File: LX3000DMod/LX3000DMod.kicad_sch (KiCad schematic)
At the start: 0 parts

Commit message: audio input terminado
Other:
- added sheet AudioSignals (AudioSignals.kicad_sch)

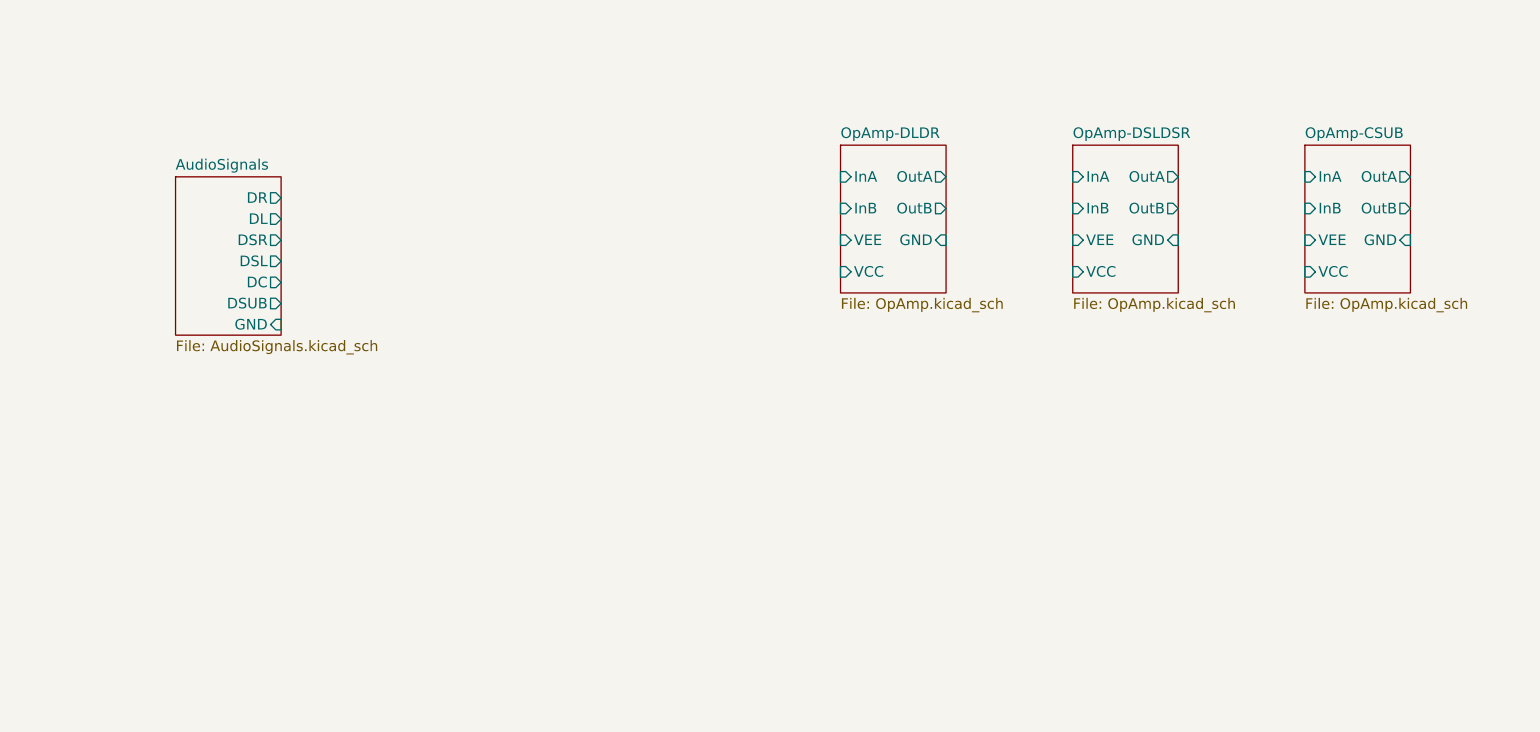
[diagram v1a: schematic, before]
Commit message: 10.8 PSU done
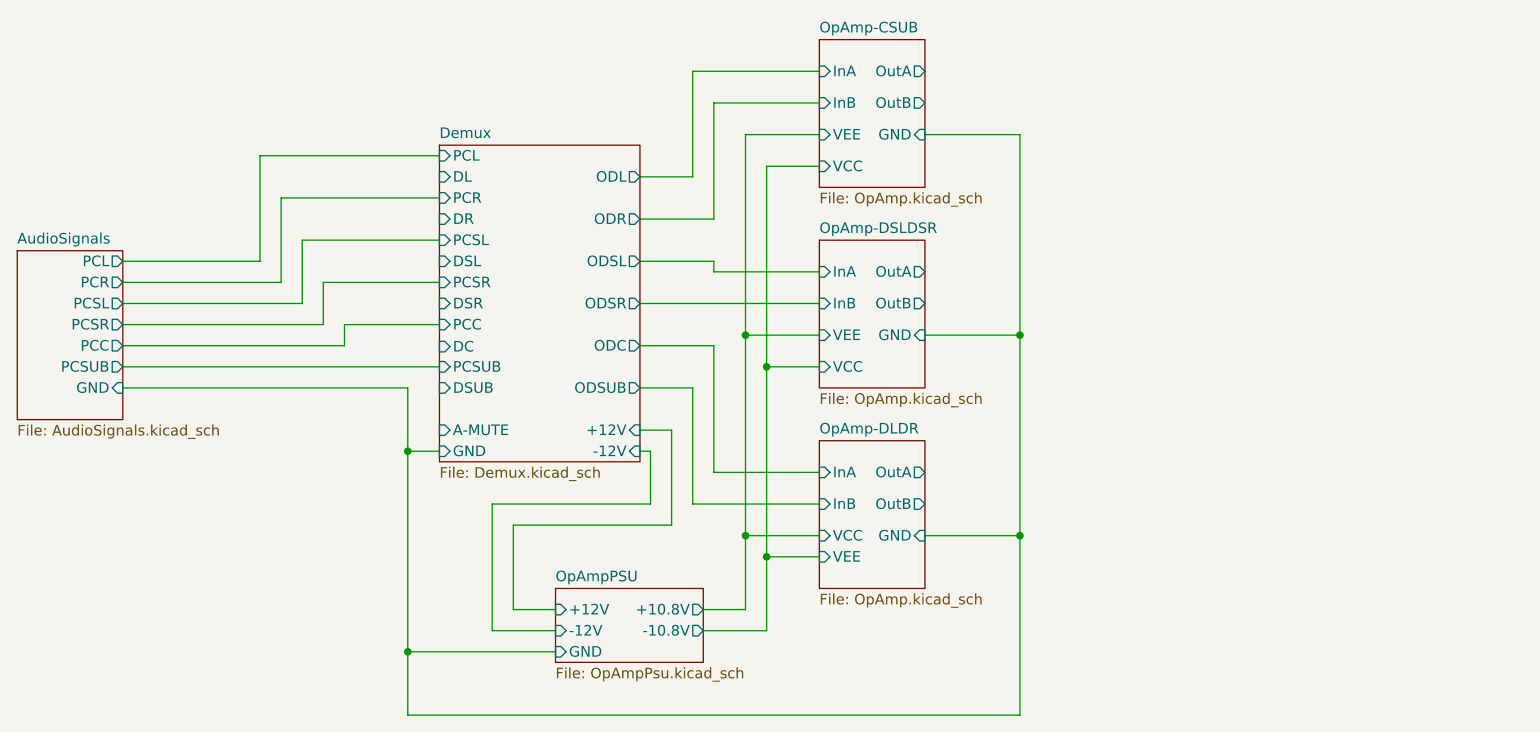
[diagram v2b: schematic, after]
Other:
- added sheet Demux (Demux.kicad_sch)
- added sheet OpAmpPSU (OpAmpPsu.kicad_sch)
- sheet AudioSignals ports: added PCC, PCL, PCR, PCSL, PCSR, PCSUB; removed DC, DL, DR, DSL, DSR, DSUB
